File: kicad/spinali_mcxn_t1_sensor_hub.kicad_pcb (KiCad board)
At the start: 4 copper layers, 182 parts, among them J1 CAN1A, J10 Debug, J11 USB4105-GF-A, J2 CAN1B, J4 5055780421, J6 CAN0A, J7 CAN0B, J8 DF40TC-50DP-0.4V(51), J9 DF40TC-50DP-0.4V(51), Q1 BUK6D56-60EX, SW1 SW_SPST, U1 MPM3811GG-Z, U10 BMM350, U11 BMP581, U12 NX5P3363UKZ, U13 SK9822-EC20, U15 TJA1462ATK, U16 PCMF3USB3S, U17 LM74700, U2 MIC5504-1.8YMT, U3 LM5160DNTJ, U4 ICM-45686, U5 MCXN947VDFT, U6 NX5P3363UKZ, U7 TJA1103AHN, U8 TJA1462ATK, Y1 25MHz, Y2 32.768kHz, Y3 24MHz

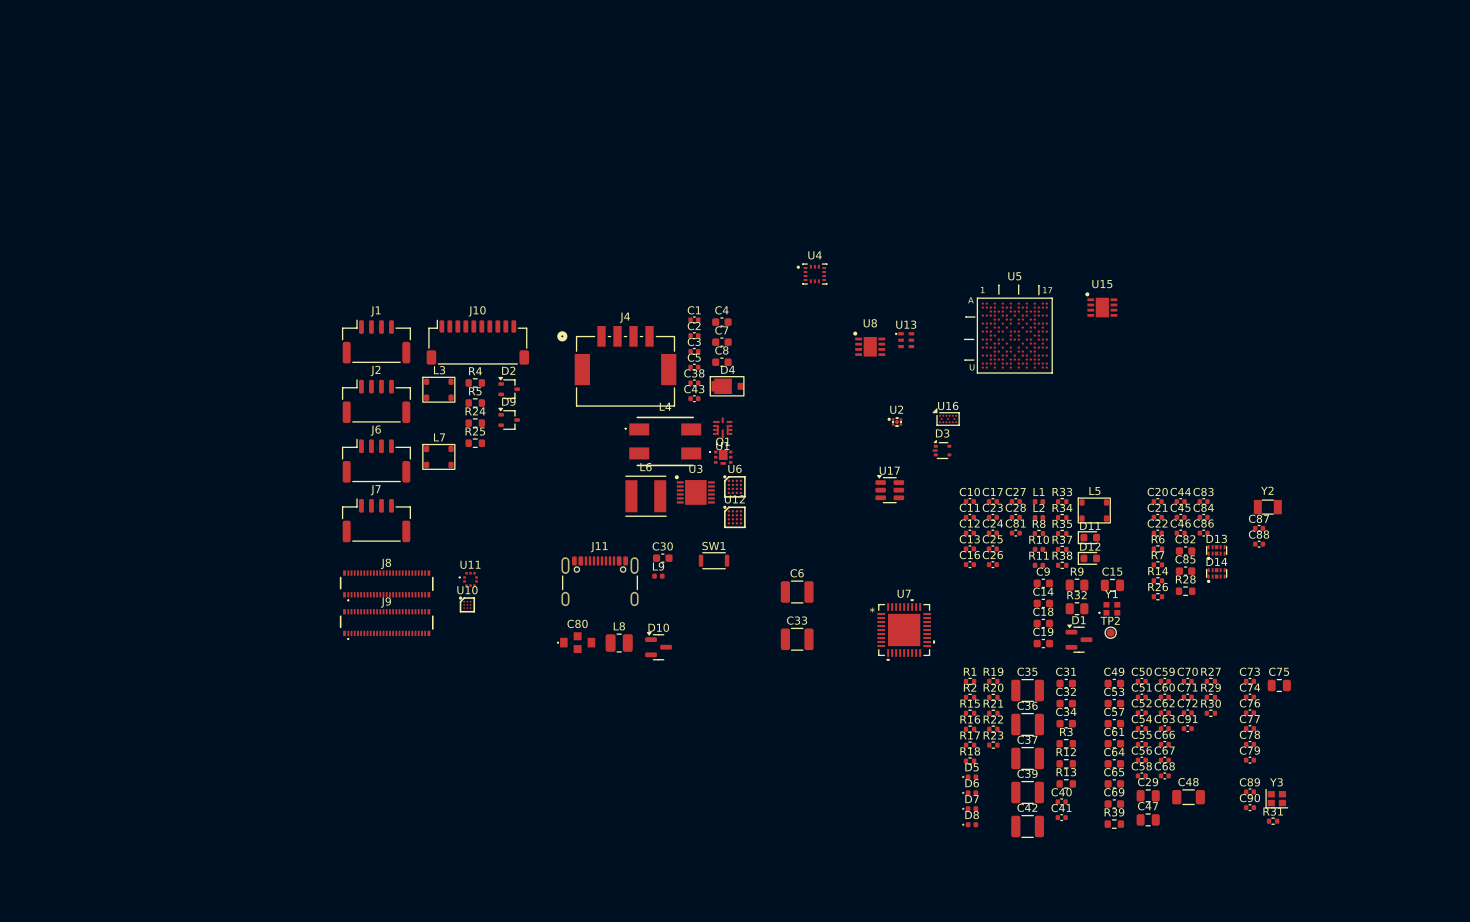
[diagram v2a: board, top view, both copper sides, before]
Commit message: Updated schematic and started on layout
- Implemented schematic changes after feedback:
	- BMM350 VDD is 1.8V
	- Replaced net labels with global labels for page references
	- Added 1uF cap to SK9822-EC20
- Added rev-RMII configuration for TJA1103 and DNP resistor to put it in slave mode
- Added TJA1103 PHY address info
- Changed decoupling caps for MCXN to smallest possible packages
- Added traces and vias at MCXN according to guidelines
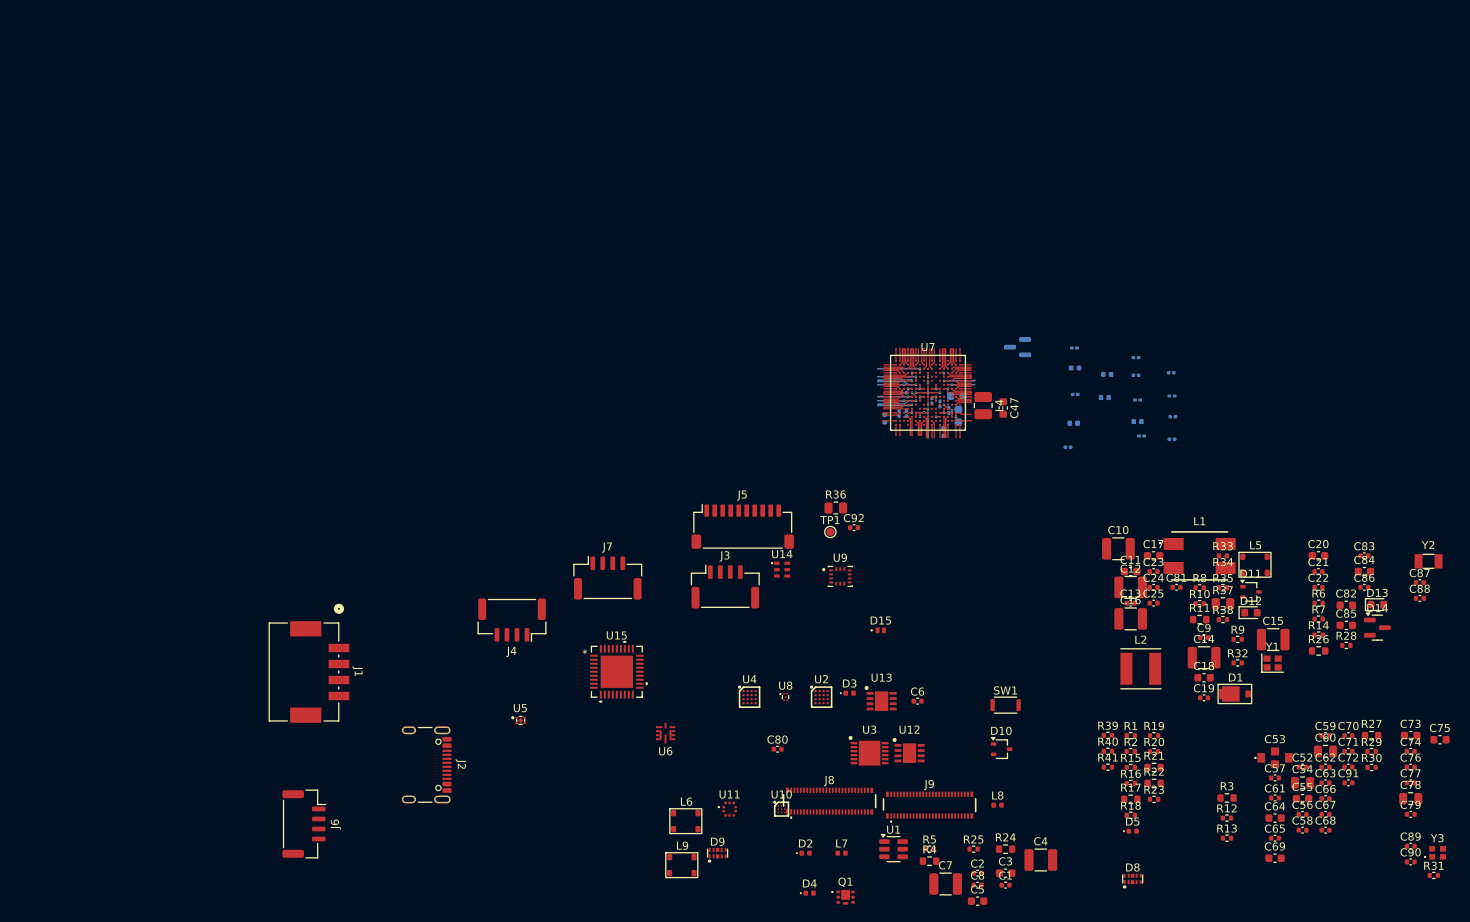
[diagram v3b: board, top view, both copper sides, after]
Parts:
- removed D7: 1V8-IND, LED_SMD:LED_0402_1005Metric
- removed J10: Debug, Connector_JST:JST_SH_SM10B-SRSS-TB_1x10-1MP_P1.00mm_Horizontal
- removed J11: USB4105-GF-A, Connector_USB:USB_C_Receptacle_GCT_USB4105-xx-A_16P_TopMnt_Horizontal
- removed TP2: ENET_REFCLK, TestPoint:TestPoint_Pad_D1.0mm
- removed U16: PCMF3USB3S, Package_CSP:Nexperia_WLCSP-15_6-3-6_2.37x1.17mm_Layout6x3_P0.4mm
- removed U17: LM74700, Package_TO_SOT_SMD:SOT-23-6
- added C92: 8pF 16V, Capacitor_SMD:C_0402_1005Metric, F.Cu at (139.8, 114.0)
- added D15: PESD5V0S1UL, TVS:PESD5V0S1ULD315, F.Cu at (143.1, 126.8)
- added J3: CAN0A, Connector_JST:JST_GH_SM04B-GHS-TB_1x04-1MP_P1.25mm_Horizontal, F.Cu at (123.7, 121.4)
- added J5: ~, Connector_JST:JST_SH_SM10B-SRSS-TB_1x10-1MP_P1.00mm_Horizontal, F.Cu at (125.8, 113.8)
- added R36: 1k 2/5W, Resistor_SMD:R_0805_2012Metric, F.Cu at (137.5, 111.5)
- added R40: 10k, Resistor_SMD:R_0402_1005Metric, F.Cu at (171.5, 141.9)
- added R41: 10k, Resistor_SMD:R_0402_1005Metric, F.Cu at (171.5, 143.9)
- added TP1: ENET_REFCLK, TestPoint:TestPoint_Pad_D1.0mm, F.Cu at (136.8, 114.5)
- added U14: SK9822-EC20, RGB_leds:SK9822EC20, F.Cu at (130.8, 119.2)
- added U9: ICM-45686, Sensors:IC_ICM-45686, F.Cu at (138.0, 120.0)
- C10: value 100nF 16V -> 10uF 100V; footprint Capacitor_SMD:C_0402_1005Metric -> Capacitor_SMD:C_1210_3225Metric
- C11: value 100nF 16V -> 100nF 100V; footprint Capacitor_SMD:C_0402_1005Metric -> Capacitor_SMD:C_0603_1608Metric
- C12, C16: value 100nF 16V -> 47uF 16V; footprint Capacitor_SMD:C_0402_1005Metric -> Capacitor_SMD:C_1210_3225Metric
- C14: value 1uF 16V -> 47uF 16V; footprint Capacitor_SMD:C_0603_1608Metric -> Capacitor_SMD:C_1210_3225Metric
- C15: value 10uF 16V -> 47uF 16V; footprint Capacitor_SMD:C_0805_2012Metric -> Capacitor_SMD:C_1210_3225Metric
- C17, C55, C73: value 100nF 16V -> 1uF 10V; footprint Capacitor_SMD:C_0402_1005Metric -> Capacitor_SMD:C_0603_1608Metric
- C18, C69: value 1uF 16V -> 1uF 10V
- C19: value 1uF 16V -> 22nF 10V; footprint Capacitor_SMD:C_0603_1608Metric -> Capacitor_SMD:C_0402_1005Metric
- C2: value 1nF 16V -> 1nF 100V
- C20: value 4700pF -> 1uF 25V; footprint Capacitor_SMD:C_0402_1005Metric -> Capacitor_SMD:C_0603_1608Metric
- C21: value 100pF -> 1nF 16V
- C22, C24: value 100pF -> 4.7pF 50V
- C23: value 100nF 50V -> 4.7pF 50V
- C25: value 4700pF 50V -> 4.7pF 50V
- C26: value 100pF -> 1uF 6.3V; moved to B.Cu
- C27: value 100nF 50V -> 100nF 10V; footprint Capacitor_SMD:C_0402_1005Metric -> Capacitor_SMD:C_0201_0603Metric; moved to B.Cu
- C28: value 8pF 16V -> 100nF 10V; footprint Capacitor_SMD:C_0402_1005Metric -> Capacitor_SMD:C_0201_0603Metric; moved to B.Cu
- C29: value 10uF 10V -> 100nF 10V; footprint Capacitor_SMD:C_0805_2012Metric -> Capacitor_SMD:C_0201_0603Metric; moved to B.Cu
- C3: value 10nF 16V -> 22nF 100V; footprint Capacitor_SMD:C_0402_1005Metric -> Capacitor_SMD:C_0603_1608Metric
- C30: value 1uF 10V -> 1uF 6.3V; footprint Capacitor_SMD:C_0603_1608Metric -> Capacitor_SMD:C_0402_1005Metric; moved to B.Cu
- C31, C34: value 100nF 100V -> 100nF 10V; footprint Capacitor_SMD:C_0603_1608Metric -> Capacitor_SMD:C_0201_0603Metric; moved to B.Cu
- C32: value 22nF 100V -> 100nF 10V; footprint Capacitor_SMD:C_0603_1608Metric -> Capacitor_SMD:C_0201_0603Metric; moved to B.Cu
- C33: value 10uF 100V -> 100nF 10V; footprint Capacitor_SMD:C_1210_3225Metric -> Capacitor_SMD:C_0201_0603Metric; moved to B.Cu
- C35, C37, C39, C42: value 47uF 16V -> 100nF 10V; footprint Capacitor_SMD:C_1210_3225Metric -> Capacitor_SMD:C_0201_0603Metric; moved to B.Cu
- C36: value 47uF 16V -> 1uF 6.3V; footprint Capacitor_SMD:C_1210_3225Metric -> Capacitor_SMD:C_0402_1005Metric; moved to B.Cu
- C38: value 1nF 100V -> 100nF 10V; footprint Capacitor_SMD:C_0402_1005Metric -> Capacitor_SMD:C_0201_0603Metric; moved to B.Cu
- C4: value 1uF 25V -> 10uF 100V; footprint Capacitor_SMD:C_0603_1608Metric -> Capacitor_SMD:C_1210_3225Metric
- C40, C41: value 100nF 16V -> 1uF 6.3V; moved to B.Cu
- C43: value 1nF 16V -> 100nF 10V; footprint Capacitor_SMD:C_0402_1005Metric -> Capacitor_SMD:C_0201_0603Metric; moved to B.Cu
- C44: value 100pF -> 100nF 10V; footprint Capacitor_SMD:C_0402_1005Metric -> Capacitor_SMD:C_0201_0603Metric; moved to B.Cu
- C45: value 4700pF -> 2.2uF 10V; moved to B.Cu
- C46: value 100pF -> 4.7uF 6.3V; footprint Capacitor_SMD:C_0402_1005Metric -> Capacitor_SMD:C_0603_1608Metric; moved to B.Cu
- C47: value 2.2uF 16V -> 10uF 6.3V; footprint Capacitor_SMD:C_0805_2012Metric -> Capacitor_SMD:C_0603_1608Metric
- C48: value 6.8uF 16V -> 100nF 10V; footprint Capacitor_SMD:C_1206_3216Metric -> Capacitor_SMD:C_0201_0603Metric; moved to B.Cu
- C49: value 1uF 16V -> 4.7uF 6.3V; moved to B.Cu
- C5: value 22nF 10V -> 100nF 100V; footprint Capacitor_SMD:C_0402_1005Metric -> Capacitor_SMD:C_0603_1608Metric
- C50, C51: value 100nF 16V -> 100nF 10V; footprint Capacitor_SMD:C_0402_1005Metric -> Capacitor_SMD:C_0201_0603Metric; moved to B.Cu
- C53: value 1uF 16V -> 15nF 50V; footprint Capacitor_SMD:C_0603_1608Metric -> Capacitors:NFM31HK103R1H3L
- C54: value 100nF 16V -> 10uF 10V; footprint Capacitor_SMD:C_0402_1005Metric -> Capacitor_SMD:C_0805_2012Metric
- C57, C61: value 1uF 16V -> 100nF 16V; footprint Capacitor_SMD:C_0603_1608Metric -> Capacitor_SMD:C_0402_1005Metric
- C6: value 10uF 100V -> 100nF 16V; footprint Capacitor_SMD:C_1210_3225Metric -> Capacitor_SMD:C_0402_1005Metric
- C60: value 100nF 16V -> 2.2uF 16V; footprint Capacitor_SMD:C_0402_1005Metric -> Capacitor_SMD:C_0805_2012Metric
- C63, C68: value 100nF 16V -> 47nF 10V
- C64: value 4.7uF 6.3V -> 1uF 10V
- C65: value 4.7uF 6.3V -> 100pF; footprint Capacitor_SMD:C_0603_1608Metric -> Capacitor_SMD:C_0402_1005Metric
- C66, C71: value 100nF 16V -> 4700pF
- C67, C70, C72: value 100nF 16V -> 100pF
- C7: value 1uF 10V -> 47uF 16V; footprint Capacitor_SMD:C_0603_1608Metric -> Capacitor_SMD:C_1210_3225Metric
- C75: value 2.2uF 16V -> 1uF 16V; footprint Capacitor_SMD:C_0805_2012Metric -> Capacitor_SMD:C_0603_1608Metric
- C78: value 100nF 16V -> 10uF 16V; footprint Capacitor_SMD:C_0402_1005Metric -> Capacitor_SMD:C_0805_2012Metric
- C8: value 1uF 10V -> 1nF 16V; footprint Capacitor_SMD:C_0603_1608Metric -> Capacitor_SMD:C_0402_1005Metric
- C80: value 15nF 50V -> 100nF 16V; footprint Capacitors:NFM31HK103R1H3L -> Capacitor_SMD:C_0402_1005Metric
- C81: value 8pF 16V -> 100nF 16V
- C82, C85: value 1uF 10V -> 1uF 16V
- C83: value 47nF 10V -> 100nF 16V
- C84: value 47nF 10V -> 1uF 16V; footprint Capacitor_SMD:C_0402_1005Metric -> Capacitor_SMD:C_0603_1608Metric
- C86: value 100nF 16V -> 100nF 50V
- C87, C89: value 4.7pF 50V -> 100pF
- C88: value 4.7pF 50V -> 4700pF 50V
- C9: value 1uF 16V -> 10nF 16V; footprint Capacitor_SMD:C_0603_1608Metric -> Capacitor_SMD:C_0402_1005Metric
- C90: value 4.7pF 50V -> 100nF 50V
- C91: value 100nF 16V -> 8pF 16V
- D1: value VETH100A203S-G3-18 -> 6DFN62CA-M3/I; footprint Package_TO_SOT_SMD:SOT-23 -> Diodes:DFN3820A
- D10: value BAT54C -> PESD2IVN24-UX; footprint Package_TO_SOT_SMD:SOT-23 -> Package_TO_SOT_SMD:SOT-323_SC-70
- D11: value LED_AMB -> PESD2IVN24-UX; footprint LED_SMD:LED_0603_1608Metric -> Package_TO_SOT_SMD:SOT-323_SC-70
- D12: value LED_GRN -> LED_AMB
- D13: value ESD7104MUTAG -> LED_GRN; footprint TVS:ESD8104MUTAG -> LED_SMD:LED_0603_1608Metric
- D14: value ESD7104MUTAG -> VETH100A203S-G3-18; footprint TVS:ESD8104MUTAG -> Package_TO_SOT_SMD:SOT-23
- D2: value PESD2IVN24-UX -> VBUS; footprint Package_TO_SOT_SMD:SOT-323_SC-70 -> LED_SMD:LED_0402_1005Metric
- D3: value PESD5V0L4UW -> 3V3-IND; footprint Package_TO_SOT_SMD:SOT-665 -> LED_SMD:LED_0402_1005Metric
- D4: value 6DFN62CA-M3/I -> 1V8-IND; footprint Diodes:DFN3820A -> LED_SMD:LED_0402_1005Metric
- D6: value 3V3-IND -> BAT54C; footprint LED_SMD:LED_0402_1005Metric -> Package_TO_SOT_SMD:SOT-23; moved to B.Cu
- D8: value VBUS -> ESD7104MUTAG; footprint LED_SMD:LED_0402_1005Metric -> TVS:ESD8104MUTAG
- D9: value PESD2IVN24-UX -> ESD7104MUTAG; footprint Package_TO_SOT_SMD:SOT-323_SC-70 -> TVS:ESD8104MUTAG
- J1: value CAN1A -> 5055780421; footprint Connector_JST:JST_GH_SM04B-GHS-TB_1x04-1MP_P1.25mm_Horizontal -> Connectors:CONN_5055780421_MOL
- J2: value CAN1B -> USB4105-GF-A; footprint Connector_JST:JST_GH_SM04B-GHS-TB_1x04-1MP_P1.25mm_Horizontal -> Connector_USB:USB_C_Receptacle_GCT_USB4105-xx-A_16P_TopMnt_Horizontal
- J4: value 5055780421 -> CAN0B; footprint Connectors:CONN_5055780421_MOL -> Connector_JST:JST_GH_SM04B-GHS-TB_1x04-1MP_P1.25mm_Horizontal
- J6: value CAN0A -> CAN1A
- J7: value CAN0B -> CAN1B
- L1: value 600 Ohm -> ACM7060-301-2PL-TL01; footprint Inductor_SMD:L_0402_1005Metric -> Inductors:ACM70603012PLTL01
- L2: value 600 Ohm -> 33uH 1.3A; footprint Inductor_SMD:L_0402_1005Metric -> Inductors:VLS5045EX330M
- L3: value IFLN1210BEER512N -> 120 Ohm; footprint Inductors:IFLN1210BEER512N -> Inductor_SMD:L_0402_1005Metric; moved to B.Cu
- L4: value ACM7060-301-2PL-TL01 -> 1.5uH; footprint Inductors:ACM70603012PLTL01 -> Inductor_SMD:L_1008_2520Metric
- L6: value VLS5045EX-330M-H -> IFLN1210BEER512N; footprint Inductors:VLS5045EX330M -> Inductors:IFLN1210BEER512N
- L7: value IFLN1210BEER512N -> 600 Ohm; footprint Inductors:IFLN1210BEER512N -> Inductor_SMD:L_0402_1005Metric
- L8: value 1.5uH -> 600 Ohm; footprint Inductor_SMD:L_1008_2520Metric -> Inductor_SMD:L_0402_1005Metric
- L9: value 120 Ohm -> IFLN1210BEER512N; footprint Inductor_SMD:L_0402_1005Metric -> Inductors:IFLN1210BEER512N
- R1: value 3k3 -> 2k2
- R10: value 680 -> 2k2; footprint Inductor_SMD:L_0402_1005Metric -> Resistor_SMD:R_0402_1005Metric
- R11: value 680 -> 12k 75V; footprint Inductor_SMD:L_0402_1005Metric -> Resistor_SMD:R_0603_1608Metric
- R12: value 68k 75V -> 2k2; footprint Resistor_SMD:R_0603_1608Metric -> Resistor_SMD:R_0402_1005Metric
- R13: value 12k 75V -> 18k 1%; footprint Resistor_SMD:R_0603_1608Metric -> Resistor_SMD:R_0402_1005Metric
- R14: value 0 -> 39k 1%
- R15, R16: value 1k -> 10k
- R17: value 82k 1% -> 100; footprint Resistor_SMD:R_0402_1005Metric -> Resistor_SMD:R_0603_1608Metric
- R18: value 18k 1% -> 5.1k
- R19: value 100k -> 5.1k
- R2: value 2k2 -> 24k 1%
- R20: value 2k2 -> 0
- R21: value 47k 1% -> 60.4R 1% 1/3W; footprint Resistor_SMD:R_0402_1005Metric -> Resistor_SMD:R_0603_1608Metric
- R22: value 2k2 -> 60.4R 1% 1/3W; footprint Resistor_SMD:R_0402_1005Metric -> Resistor_SMD:R_0603_1608Metric
- R23: value 24k 1% -> 0
- R24: value 60.4R 1% 1/3W -> 100
- R25: value 60.4R 1% 1/3W -> 0; footprint Resistor_SMD:R_0603_1608Metric -> Resistor_SMD:R_0402_1005Metric
- R26: value 0 -> 60.4R 1% 1/3W; footprint Resistor_SMD:R_0402_1005Metric -> Resistor_SMD:R_0603_1608Metric
- R27: value 10k -> 60.4R 1% 1/3W; footprint Resistor_SMD:R_0402_1005Metric -> Resistor_SMD:R_0603_1608Metric
- R28: value 100 -> 0; footprint Resistor_SMD:R_0603_1608Metric -> Resistor_SMD:R_0402_1005Metric
- R29, R30: value 5.1k -> 10k
- R32: value 1k 2/5W -> 10k; footprint Resistor_SMD:R_0805_2012Metric -> Resistor_SMD:R_0402_1005Metric
- R33: value 0 -> 680; footprint Resistor_SMD:R_0402_1005Metric -> Inductor_SMD:L_0402_1005Metric
- R34: value 10k -> 680; footprint Resistor_SMD:R_0402_1005Metric -> Inductor_SMD:L_0402_1005Metric
- R35, R38: value 10k -> 0
- R37: value 10k -> 1k 2/5W; footprint Resistor_SMD:R_0402_1005Metric -> Resistor_SMD:R_0805_2012Metric
- R39: value 100 -> 10k; footprint Resistor_SMD:R_0603_1608Metric -> Resistor_SMD:R_0402_1005Metric
- R4: value 60.4R 1% 1/3W -> 68k 75V
- R5: value 60.4R 1% 1/3W -> 3k3; footprint Resistor_SMD:R_0603_1608Metric -> Resistor_SMD:R_0402_1005Metric
- R6: value 0 -> 100k
- R7: value 0 -> 82k 1%
- R8: value 0 -> 1k
- R9: value 1k 2/5W -> 1k; footprint Resistor_SMD:R_0805_2012Metric -> Resistor_SMD:R_0402_1005Metric
- U1: value MPM3811GG-Z -> LM74700; footprint Power:QFN2x2x1p6_MPM3811_MNP -> Package_TO_SOT_SMD:SOT-23-6
- U12: value NX5P3363UKZ -> TJA1462ATK; footprint NXP_BGA:BGA16C50P4X4_220X220X60 -> NXP_HV:SON65P300X300X100-9N-D
- U13: value SK9822-EC20 -> TJA1462ATK; footprint RGB_leds:SK9822EC20 -> NXP_HV:SON65P300X300X100-9N-D
- U15: value TJA1462ATK -> TJA1103AHN; footprint NXP_HV:SON65P300X300X100-9N-D -> NXP_HV:HVQFN36_SOT1092-2_NXP
- U2: value MIC5504-1.8YMT -> NX5P3363UKZ; footprint Power:VREG_MIC5504-3.3YMT-TZ -> NXP_BGA:BGA16C50P4X4_220X220X60
- U4: value ICM-45686 -> NX5P3363UKZ; footprint Sensors:IC_ICM-45686 -> NXP_BGA:BGA16C50P4X4_220X220X60
- U5: value MCXN947VDFT -> MIC5504-1.8YMT; footprint NXP_BGA:BGA184_0P5_9X9_SM -> Power:VREG_MIC5504-3.3YMT-TZ
- U6: value NX5P3363UKZ -> MPM3811GG-Z; footprint NXP_BGA:BGA16C50P4X4_220X220X60 -> Power:QFN2x2x1p6_MPM3811_MNP
- U7: value TJA1103AHN -> MCXN947VDFT; footprint NXP_HV:HVQFN36_SOT1092-2_NXP -> NXP_BGA:BGA184_0P5_9X9_SM
- U8: value TJA1462ATK -> PCMF1USB3SZ; footprint NXP_HV:SON65P300X300X100-9N-D -> TVS:PESD1USB3BCX
- Y1: value 25MHz -> 24MHz; footprint Crystals:XRCGB25M000F3A00R0 -> Crystal:Crystal_SMD_2016-4Pin_2.0x1.6mm
- Y3: value 24MHz -> 25MHz; footprint Crystal:Crystal_SMD_2016-4Pin_2.0x1.6mm -> Crystals:XRCGB25M000F3A00R0
- moved R24 85.0 mm to (158.7, 154.1)
- moved R4 82.5 mm to (149.2, 155.6)
- moved L3 81.0 mm to (167.2, 100.9), turned to 180 degrees
- moved C1 80.7 mm to (158.7, 158.6)
- moved R25 80.3 mm to (154.7, 154.1)
- moved R5 79.6 mm to (149.2, 154.1)
- moved U5 78.3 mm to (98.1, 138.1)
- moved C4 78.2 mm to (163.1, 155.5)
- moved C2 75.9 mm to (155.2, 157.1)
- moved C3 75.9 mm to (158.7, 157.1)
- moved U15 75.9 mm to (110.1, 132.0)
- moved C5 75.6 mm to (155.2, 160.6)
- moved C7 73.3 mm to (151.2, 158.5)
- moved C8 72.8 mm to (155.2, 158.6)
- moved L7 72.4 mm to (138.2, 154.6)
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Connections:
- net /Board-to-Board/P0_23/FLEXIO0_D7 renamed P0_23/FLEXIO0_D7
- C1 pad 1: Net-(Q1-S) -> Net-(C1-Pad1)
- C10 pad 2: VDDIO -> +BATT
- C11 pad 2: VDDIO -> +BATT
- C12 pad 1: Net-(U7-VDDA_AO) -> GND
- C12 pad 2: GND -> Net-(U4-EN)
- C13 pad 1: GND -> Net-(U4-EN)
- C13 pad 2: Net-(U7-VDDA_AO) -> GND
- C14 pad 2: Net-(U7-VDDA_AO) -> +5V
- C15 pad 2: Net-(U7-VDD_CORE) -> +5V
- C16 pad 2: Net-(U7-VDD_CORE) -> +3V3
- C17 pad 1: GND -> +3V3
- C17 pad 2: VDDA_TRX -> GND
- C18 pad 1: GND -> +1V8
- C18 pad 2: VDDA_TRX -> GND
- C19 pad 2: VDDA_TRX -> Net-(U3-SS)
- C2 pad 1: GND -> Net-(Q1-S)
- C2 pad 2: Net-(U6-CAP) -> GND
- C20 pad 2: Net-(C20-Pad2) -> Net-(U3-VCC)
- C21 pad 1: Net-(D9-A2) -> GND
- C21 pad 2: GND -> Net-(U4-CAP)
- C22 pad 2: Net-(D9-A1) -> /MCU IO Part 1/XTAL48M
- C23 pad 1: Net-(C23-Pad1) -> GND
- C23 pad 2: /Ethernet PHY/ENET_TRX_P -> /MCU IO Part 1/EXTAL48M
- C24 pad 1: GND -> /MCU IO Part 2/P5_0/EXTAL32K
- C24 pad 2: /Ethernet PHY/ENET_TRX_P -> GND
- C25 pad 1: GND -> /MCU IO Part 2/P5_1/XTAL32K
- C25 pad 2: Net-(C25-Pad2) -> GND
- C26 pad 1: /Ethernet PHY/ENET_TRX_M -> +3V3
- C27 pad 1: Net-(C27-Pad1) -> +3V3
- C27 pad 2: /Ethernet PHY/ENET_TRX_M -> GND
- C28 pad 1: /Ethernet PHY/ENET0_XTAL_IN -> +3V3
- C29 pad 1: VBUS -> +3V3
- C3 pad 1: Net-(U3-BST) -> GND
- C3 pad 2: Net-(C3-Pad2) -> Net-(Q1-S)
- C30 pad 1: VBUS -> +3V3
- C31 pad 1: Net-(U17-VCAP) -> +3V3
- C31 pad 2: Net-(Q1-S) -> GND
- C32 pad 1: GND -> +3V3
- C32 pad 2: Net-(Q1-S) -> GND
- C33 pad 2: +BATT -> +3V3
- C34 pad 2: +BATT -> Net-(U7H-VDD_BAT)
- C35 pad 2: Net-(U6-EN) -> Net-(U7H-VDD_ANA)
- C36 pad 1: GND -> +3V3
- C36 pad 2: +3V3 -> GND
- C37 pad 1: GND -> +3V3
- C37 pad 2: +5V -> GND
- C38 pad 1: Net-(C38-Pad1) -> +3V3
- C39 pad 1: GND -> +3V3
- C39 pad 2: +5V -> GND
- C4 pad 2: Net-(U3-VCC) -> +BATT
- C40 pad 1: Net-(U6-EN) -> GND
- C40 pad 2: GND -> Net-(U7H-VDD_ANA)
- C41 pad 1: VBUS -> +3V3
- C42 pad 1: GND -> +3V3
- C42 pad 2: +5V -> GND
- C43 pad 1: GND -> +3V3
- C43 pad 2: Net-(U12-CAP) -> GND
- C44 pad 2: Net-(D2-A1) -> +3V3
- C45 pad 1: GND -> Net-(U7H-VDD_SYS/VOUT_SYS)
- C45 pad 2: Net-(C45-Pad2) -> GND
- C46 pad 1: Net-(D2-A2) -> +3V3
- C47 pad 1: Net-(U5H-VDD_SYS/VOUT_SYS) -> Net-(U7H-VDD_CORE_1)
- C48 pad 1: Net-(U5H-VDD_CORE_1) -> GND
- C48 pad 2: GND -> Net-(U7H-VDD_CORE_1)
- C49 pad 1: +3V3 -> Net-(U7H-VDD_CORE_1)
- C5 pad 1: GND -> Net-(U1-VCAP)
- C5 pad 2: Net-(U3-SS) -> Net-(Q1-S)
- C50 pad 1: +3V3 -> Net-(U7H-VDD_CORE_1)
- C51 pad 1: +3V3 -> Net-(U7H-VDD_CORE_1)
- C52 pad 1: +3V3 -> RESET_b
- C53 pad 1: +3V3 -> Net-(D15-K1)
- C54 pad 1: +3V3 -> VBUS
- C55 pad 1: +3V3 -> VBUS
- C56 pad 1: GND -> +3V3
- C56 pad 2: +3V3 -> GND
- C59 pad 1: +3V3 -> +1V8
- C6 pad 1: GND -> VBUS
- C6 pad 2: +BATT -> GND
- C60 pad 1: +3V3 -> Net-(U10-CRST)
- C61 pad 1: +3V3 -> GND
- C61 pad 2: GND -> +3V3
- C62 pad 1: +3V3 -> GND
- C62 pad 2: GND -> +3V3
- C64 pad 1: +3V3 -> +5V
- C65 pad 1: Net-(U5H-VDD_CORE_1) -> GND
- C65 pad 2: GND -> Net-(D10-A1)
- C66 pad 1: Net-(U5H-VDD_CORE_1) -> GND
- C66 pad 2: GND -> Net-(C66-Pad2)
- C67 pad 1: Net-(U5H-VDD_CORE_1) -> Net-(D10-A2)
- C68 pad 1: GND -> +3V3
- C68 pad 2: Net-(U5H-VDD_CORE_1) -> GND
- C69 pad 1: GND -> +5V
- C69 pad 2: Net-(U5H-VDD_ANA) -> GND
- C7 pad 1: +3V3 -> GND
- C7 pad 2: GND -> +5V
- C70 pad 2: Net-(U5H-VDD_ANA) -> Net-(D11-A1)
- C71 pad 2: +3V3 -> Net-(C71-Pad2)
- C72 pad 1: GND -> Net-(D11-A2)
- C72 pad 2: Net-(U5H-VDD_BAT) -> GND
- C73 pad 2: +3V3 -> +5V
- C74 pad 2: +3V3 -> +5V
- C75 pad 1: Net-(U10-CRST) -> GND
- C75 pad 2: GND -> VDDIO
- C76 pad 1: +3V3 -> GND
- C76 pad 2: GND -> VDDIO
- C77 pad 1: +3V3 -> GND
- C77 pad 2: GND -> VDDIO
- C78 pad 1: +3V3 -> GND
- C78 pad 2: GND -> Net-(U15-VDD_CORE)
- C79 pad 1: +3V3 -> GND
- C79 pad 2: GND -> Net-(U15-VDD_CORE)
- C8 pad 1: +1V8 -> GND
- C8 pad 2: GND -> Net-(U2-CAP)
- C80 pad 1: Net-(D3A-K1) -> Net-(U15-VDDA_AO)
- C81 pad 1: /Ethernet PHY/ENET0_XTAL_OUT -> GND
- C81 pad 2: GND -> Net-(U15-VDDA_AO)
- C82 pad 1: +5V -> GND
- C82 pad 2: GND -> Net-(U15-VDDA_AO)
- C83 pad 1: +3V3 -> GND
- C83 pad 2: GND -> VDDA_TRX
- C84 pad 1: +3V3 -> GND
- C84 pad 2: GND -> VDDA_TRX
- C85 pad 1: +5V -> GND
- C85 pad 2: GND -> VDDA_TRX
- C86 pad 1: +5V -> Net-(C86-Pad1)
- C86 pad 2: GND -> ENET0_TRX_P
- C87 pad 1: /MCU IO Part 2/P5_1/XTAL32K -> GND
- C87 pad 2: GND -> ENET0_TRX_P
- C88 pad 1: /MCU IO Part 2/P5_0/EXTAL32K -> GND
- C88 pad 2: GND -> Net-(C88-Pad2)
- C89 pad 1: GND -> ENET0_TRX_M
- C89 pad 2: /MCU IO Part 1/XTAL48M -> GND
- C9 pad 1: GND -> Net-(U3-BST)
- C9 pad 2: VDDIO -> Net-(C9-Pad2)
- C90 pad 1: GND -> Net-(C90-Pad1)
- C90 pad 2: /MCU IO Part 1/EXTAL48M -> ENET0_TRX_M
- C91 pad 1: /MCU IO USB & Power/RESET_b -> /Ethernet PHY/ENET0_XTAL_IN
- D1 pad 1: /Ethernet PHY/ENET_TRX_P -> GND
- D1 pad 2: /Ethernet PHY/ENET_TRX_M -> Net-(C1-Pad1)
- D10 pad 1: /MCU IO USB & Power/VDD_BAT -> Net-(D10-A1)
- D10 pad 2: +3V3 -> Net-(D10-A2)
- D10 pad 3: Net-(U5H-VDD_BAT) -> GND
- D11 pad 1: GND -> Net-(D11-A1)
- D11 pad 2: Net-(D11-A) -> Net-(D11-A2)
- D13 pad 1: /Communication/P0_1/DEBUG_TCLK_SWCLK -> GND
- D13 pad 2: /Communication/P0_0/DEBUG_TMS_SWDIO -> Net-(D13-A)
- D14 pad 1: /Communication/RESET_b -> ENET0_TRX_P
- D14 pad 2: /Communication/P0_4 -> ENET0_TRX_M
- D2 pad 1: Net-(D2-A1) -> GND
- D2 pad 2: Net-(D2-A2) -> Net-(D2-A)
- D3 pad 1: Net-(D3A-K1) -> GND
- D3 pad 2: GND -> Net-(D3-A)
- D4 pad 2: Net-(C38-Pad1) -> Net-(D4-A)
- D6 pad 1: GND -> VDD_BAT
- D6 pad 2: Net-(D6-A) -> +3V3
- D8 pad 1: GND -> P0_1/DEBUG_TCLK_SWCLK
- D8 pad 2: Net-(D8-A) -> P0_0/DEBUG_TMS_SWDIO
- D9 pad 1: Net-(D9-A1) -> RESET_b
- D9 pad 2: Net-(D9-A2) -> P0_4
- J1 pad 1: Net-(J1-Pin_1) -> Net-(C1-Pad1)
- J1 pad 2: Net-(D9-A1) -> ENET0_TRX_P
- J1 pad 3: Net-(D9-A2) -> ENET0_TRX_M
- J4 pad 1: Net-(C38-Pad1) -> Net-(J3-Pad1)
- J4 pad 2: /Power supplies/ENET_TRX_P -> Net-(D10-A1)
- J4 pad 3: /Power supplies/ENET_TRX_M -> Net-(D10-A2)
- J6 pad 2: Net-(D2-A1) -> Net-(D11-A1)
- J6 pad 3: Net-(D2-A2) -> Net-(D11-A2)
- J6 pad MP: (no net) -> GND
- J7 pad 2: Net-(D2-A1) -> Net-(D11-A1)
- J7 pad 3: Net-(D2-A2) -> Net-(D11-A2)
- J7 pad MP: (no net) -> GND
- J8 pad 11: /Board-to-Board/VDD_BAT -> VDD_BAT
- J8 pad 14: /Board-to-Board/P1_8/I3C1_SDA/FC4_P0 -> P1_8/I3C1_SDA/FC4_P0
- J8 pad 16: /Board-to-Board/P1_9/I3C1_SCL/FC4_P1 -> P1_9/I3C1_SCL/FC4_P1
- J8 pad 20: /Board-to-Board/P1_22/FC4_P2 -> P1_22/FC4_P2
- J8 pad 21: /Board-to-Board/P4_0/FC2_P0 -> P4_0/FC2_P0
- J8 pad 22: /Board-to-Board/P1_23/FC4_P3 -> P1_23/FC4_P3
- J8 pad 23: /Board-to-Board/P4_1/FC2_P1 -> P4_1/FC2_P1
- J8 pad 26: /Board-to-Board/P3_1/FC6_P0 -> P3_1/FC6_P0
- J8 pad 27: /Board-to-Board/P4_2/FC2_P2 -> P4_2/FC2_P2
- J8 pad 28: /Board-to-Board/P3_6/FC6_P1 -> P3_6/FC6_P1
- J8 pad 29: /Board-to-Board/P4_3/FC2_P3 -> P4_3/FC2_P3
- J8 pad 32: /Board-to-Board/P3_10/FC6_P2 -> P3_10/FC6_P2
- J8 pad 33: /Board-to-Board/P4_23/FC2_P6 -> P4_23/FC2_P6
- J8 pad 34: /Board-to-Board/P3_11/FC6_P3 -> P3_11/FC6_P3
- J8 pad 35: /Board-to-Board/P4_20/FC2_P4 -> P4_20/FC2_P4
- J8 pad 38: /Board-to-Board/P3_18/FC6_P6 -> P3_18/FC6_P6
- J8 pad 39: /Board-to-Board/ANA_22/OPAMP2_INN -> ANA_22/OPAMP2_INN
- J8 pad 40: /Board-to-Board/P3_13/FC6_P5 -> P3_13/FC6_P5
- J8 pad 41: /Board-to-Board/ANA_6/DAC2_OUT -> ANA_6/DAC2_OUT
- J8 pad 44: /Board-to-Board/P2_10/TRACE_DATA2 -> P2_10/TRACE_DATA2
- J8 pad 46: /Board-to-Board/P2_11/TRACE_DATA3 -> P2_11/TRACE_DATA3
- J8 pad 47: /Board-to-Board/P3_21/FLEXIO0_D29 -> P3_21/FLEXIO0_D29
- J9 pad 10: /Board-to-Board/P3_8/SmartDMA_PIO8 -> P3_8/SmartDMA_PIO8
- J9 pad 11: /Board-to-Board/P2_2/SDHC0_D1 -> P2_2/SDHC0_D1
- J9 pad 12: /Board-to-Board/P3_9/SmartDMA_PIO9 -> P3_9/SmartDMA_PIO9
- J9 pad 15: /Board-to-Board/P2_7/SDHC0_D2 -> P2_7/SDHC0_D2
- J9 pad 16: /Board-to-Board/P1_0/FC3_P0 -> P1_0/FC3_P0
- J9 pad 17: /Board-to-Board/P2_6/SDHC0_D3 -> P2_6/SDHC0_D3
- J9 pad 18: /Board-to-Board/P1_1/FC3_P1 -> P1_1/FC3_P1
- J9 pad 21: /Board-to-Board/P2_1/SDHC0_D4 -> P2_1/SDHC0_D4
- J9 pad 22: /Board-to-Board/P1_2/FC3_P2 -> P1_2/FC3_P2
- J9 pad 23: /Board-to-Board/P2_0/SDHC0_D5 -> P2_0/SDHC0_D5
- J9 pad 24: /Board-to-Board/P1_3/FC3_P3 -> P1_3/FC3_P3
- J9 pad 27: /Board-to-Board/P2_9/SDHC0_D6 -> P2_9/SDHC0_D6
- J9 pad 28: /Board-to-Board/P1_18/FC3_P6 -> P1_18/FC3_P6
- J9 pad 29: /Board-to-Board/P2_8/SDHC0_D7 -> P2_8/SDHC0_D7
- J9 pad 3: /Board-to-Board/P2_5/SDHC0_CMD -> P2_5/SDHC0_CMD
- J9 pad 32: /Board-to-Board/P1_16/FC3_P4 -> P1_16/FC3_P4
- J9 pad 33: /Board-to-Board/P3_2/FC7_P0 -> P3_2/FC7_P0
- J9 pad 34: /Board-to-Board/P1_17/FC3_P5 -> P1_17/FC3_P5
- J9 pad 35: /Board-to-Board/P3_3/FC7_P1 -> P3_3/FC7_P1
- J9 pad 38: /Board-to-Board/P0_16/FC0_P0 -> P0_16/FC0_P0
- J9 pad 39: /Board-to-Board/P3_4/FC7_P2 -> P3_4/FC7_P2
- J9 pad 4: /Board-to-Board/P3_0/SmartDMA_PIO0 -> P3_0/SmartDMA_PIO0
- J9 pad 40: /Board-to-Board/P0_17/FC0_P1 -> P0_17/FC0_P1
- J9 pad 41: /Board-to-Board/P3_5/FC7_P3 -> P3_5/FC7_P3
- J9 pad 44: /Board-to-Board/P0_18/FC0_P2 -> P0_18/FC0_P2
- J9 pad 45: /Board-to-Board/P3_19/FC7_P6 -> P3_19/FC7_P6
- J9 pad 46: /Board-to-Board/P0_7/FC0_P3 -> P0_7/FC0_P3
- J9 pad 47: /Board-to-Board/P3_12/FC7_P4 -> P3_12/FC7_P4
- J9 pad 48: /Board-to-Board/P0_22/FC0_P6 -> P0_22/FC0_P6
- J9 pad 5: /Board-to-Board/P2_4/SDHC0_CLK -> P2_4/SDHC0_CLK
- J9 pad 6: /Board-to-Board/P3_7/SmartDMA_PIO7 -> P3_7/SmartDMA_PIO7
- J9 pad 9: /Board-to-Board/P2_3/SDHC0_D0 -> P2_3/SDHC0_D0
- L1 pad 1: +3V3 -> Net-(C1-Pad1)
- L1 pad 2: VDDIO -> GND
- L2 pad 1: +3V3 -> Net-(C9-Pad2)
- L2 pad 2: Net-(U7-VDDA_AO) -> Net-(U4-EN)
- L3 pad 1: Net-(U8-CANH) -> +3V3
- L3 pad 2: Net-(D2-A1) -> Net-(U7H-VDD_ANA)
- L4 pad 1: Net-(C38-Pad1) -> Net-(U7H-VDD_CORE_1)
- L4 pad 2: GND -> Net-(U7H-DCDC_LX/DCDC_LX)
- L5 pad 1: /Ethernet PHY/TRX_P -> Net-(U12-CANH)
- L5 pad 2: Net-(C23-Pad1) -> Net-(D10-A1)
- L5 pad 3: Net-(C27-Pad1) -> Net-(D10-A2)
- L5 pad 4: /Ethernet PHY/TRX_M -> Net-(U12-CANL)
- L6 pad 1: Net-(C3-Pad2) -> Net-(U13-CANH)
- L6 pad 2: Net-(U6-EN) -> Net-(D11-A1)
- L7 pad 1: Net-(U15-CANH) -> +3V3
- L7 pad 2: Net-(D9-A1) -> VDDIO
- L8 pad 1: Net-(U5H-VDD_CORE_1) -> +3V3
- L8 pad 2: Net-(U5H-DCDC_LX/DCDC_LX) -> Net-(U15-VDDA_AO)
- L9 pad 1: +3V3 -> /Ethernet PHY/TRX_P
- L9 pad 2: Net-(U5H-VDD_ANA) -> Net-(C86-Pad1)
- R1 pad 1: Net-(U6-EN) -> VBUS
- R1 pad 2: Net-(U3-FB) -> Net-(D2-A)
- R10 pad 1: Net-(U7-TMS/GPIO0/CONFIG0) -> Net-(U4-EN)
- R10 pad 2: Net-(D11-A) -> Net-(D5-A)
- R11 pad 1: Net-(U7-TDI/GPIO1) -> Net-(U3-EN/UVLO)
- R11 pad 2: Net-(D12-A) -> GND
- R12 pad 1: +BATT -> Net-(U3-FB)
- R12 pad 2: Net-(U3-EN/UVLO) -> GND
- R13 pad 1: Net-(U3-EN/UVLO) -> Net-(U6-FB)
- R14 pad 1: Net-(U8-CANH) -> Net-(U4-ILIM)
- R14 pad 2: Net-(D2-A1) -> GND
- R15 pad 1: +1V8 -> +3V3
- R15 pad 2: Net-(D7-A) -> /MCU IO Part 1/P0_6/ISPMODE_N
- R16 pad 2: Net-(D6-A) -> RESET_b
- R17 pad 1: +3V3 -> Net-(U7G-RESET_b)
- R17 pad 2: Net-(U1-FB) -> RESET_b
- R18 pad 1: Net-(U1-FB) -> Net-(J2-CC1)
- R19 pad 1: +5V -> GND
- R19 pad 2: Net-(U1-EN) -> Net-(J2-CC2)
- R2 pad 1: Net-(U3-FB) -> Net-(U2-ILIM)
- R20 pad 1: Net-(U6-EN) -> Net-(U12-CANH)
- R20 pad 2: Net-(D5-A) -> Net-(D10-A1)
- R21 pad 1: Net-(U6-ILIM) -> Net-(D10-A1)
- R21 pad 2: GND -> Net-(C66-Pad2)
- R22 pad 1: VBUS -> Net-(C66-Pad2)
- R22 pad 2: Net-(D8-A) -> Net-(D10-A2)
- R23 pad 1: Net-(U12-ILIM) -> Net-(D10-A2)
- R23 pad 2: GND -> Net-(U12-CANL)
- R24 pad 1: Net-(D2-A1) -> +3V3
- R24 pad 2: Net-(C45-Pad2) -> Net-(J5-Pad1)
- R25 pad 1: Net-(C45-Pad2) -> Net-(U13-CANH)
- R25 pad 2: Net-(D2-A2) -> Net-(D11-A1)
- R26 pad 1: Net-(D2-A2) -> Net-(D11-A1)
- R26 pad 2: Net-(U8-CANL) -> Net-(C71-Pad2)
- R27 pad 1: +3V3 -> Net-(C71-Pad2)
- R27 pad 2: /MCU IO USB & Power/RESET_b -> Net-(D11-A2)
- R28 pad 1: +3V3 -> Net-(D11-A2)
- R28 pad 2: Net-(J10-Pin_1) -> Net-(U13-CANL)
- R29 pad 1: Net-(J11-CC1) -> +3V3
- R29 pad 2: GND -> P1_19/ENET0_INT_N
- R30 pad 1: GND -> +3V3
- R30 pad 2: Net-(J11-CC2) -> P1_21/ENET0_MDIO
- R31 pad 2: /MCU IO Part 1/P0_6/ISPMODE_N -> P1_11/ENET0_NRST
- R32 pad 1: Net-(C25-Pad2) -> P0_31/ENET0_WAKE_IN_OUT
- R32 pad 2: /Ethernet PHY/ENET_TRX_M -> GND
- R33 pad 1: Net-(C27-Pad1) -> Net-(U15-TMS/GPIO0/CONFIG0)
- R33 pad 2: /Ethernet PHY/TRX_M -> Net-(D12-A)
- R34 pad 1: +3V3 -> Net-(U15-TDI/GPIO1)
- R34 pad 2: /Ethernet PHY/ENET0_NRST -> Net-(D13-A)
- R35 pad 1: +3V3 -> /Ethernet PHY/TRX_P
- R35 pad 2: /Ethernet PHY/P1_21/ENET0_MDIO -> Net-(C86-Pad1)
- R37 pad 1: +3V3 -> Net-(C88-Pad2)
- R37 pad 2: /Ethernet PHY/P1_19/ENET0_INT_N -> ENET0_TRX_M
- R38 pad 1: /Ethernet PHY/P0_31/ENET0_WAKE_IN_OUT -> Net-(C90-Pad1)
- R38 pad 2: GND -> /Ethernet PHY/TRX_M
- R39 pad 1: Net-(U5G-RESET_b) -> +3V3
- R39 pad 2: /MCU IO USB & Power/RESET_b -> Net-(U15-RXD2/GPIO4/CONFIG3)
- R4 pad 1: Net-(D9-A1) -> +BATT
- R4 pad 2: Net-(C20-Pad2) -> Net-(U3-EN/UVLO)
- R5 pad 1: Net-(C20-Pad2) -> Net-(U4-EN)
- R5 pad 2: Net-(D9-A2) -> Net-(U3-FB)
- R6 pad 1: Net-(U15-CANH) -> +5V
- R6 pad 2: Net-(D9-A1) -> Net-(U6-EN)
- R7 pad 1: Net-(D9-A2) -> +3V3
- R7 pad 2: Net-(U15-CANL) -> Net-(U6-FB)
- R8 pad 1: /Ethernet PHY/TRX_P -> +3V3
- R8 pad 2: Net-(C23-Pad1) -> Net-(D3-A)
- R9 pad 1: /Ethernet PHY/ENET_TRX_P -> +1V8
- R9 pad 2: Net-(C25-Pad2) -> Net-(D4-A)
- U1 pad 1: +5V -> Net-(U1-VCAP)
- U1 pad 2: unconnected-(U1-SW-Pad2)_1 -> GND
- U1 pad 3: unconnected-(U1-SW-Pad2)_2 -> Net-(Q1-S)
- U1 pad 4: unconnected-(U1-SW-Pad2) -> +BATT
- U1 pad 5: Net-(U1-EN) -> Net-(Q1-G)
- U1 pad 6: +3V3 -> Net-(Q1-S)
- U10 pad A2: /Sensors/P0_20/I3C0_SDA -> P0_20/I3C0_SDA
- U10 pad A3: /Sensors/P0_21/I3C0_SCL -> P0_21/I3C0_SCL
- U10 pad C1: +3V3 -> +1V8
- U11 pad 2: /Sensors/P0_21/I3C0_SCL -> P0_21/I3C0_SCL
- U11 pad 5: /Sensors/P0_20/I3C0_SDA -> P0_20/I3C0_SDA
- U13 pad 1: unconnected-(U13-SDO-Pad1) -> P4_16/CAN1_TXD
- U13 pad 3: /Communication/P0_8/FLEXIO0_D0 -> +5V
- U13 pad 4: /Communication/P0_9/FLEXIO0_D1 -> P4_15/CAN1_RXD
- U13 pad 5: +5V -> +3V3
- U13 pad 6: unconnected-(U13-CKO-Pad6) -> Net-(U13-CANL)
- U15 pad 1: /Communication/CAN1_TXD -> P1_20/ENET0_MDC
- U15 pad 2: GND -> P1_19/ENET0_INT_N
- U15 pad 3: +5V -> Net-(U15-VDD_CORE)
- U15 pad 4: /Communication/CAN1_RXD -> VDDIO
- U15 pad 5: +3V3 -> /Ethernet PHY/ENET0_XTAL_OUT
- U15 pad 6: Net-(U15-CANL) -> /Ethernet PHY/ENET0_XTAL_IN
- U15 pad 7: Net-(U15-CANH) -> Net-(U15-VDDA_AO)
- U15 pad 8: /Communication/MCU_P2_11 -> VDDA_TRX
- U15 pad 9: GND -> Net-(U15-VDDA_AO)
- U3 pad 11: Net-(C3-Pad2) -> Net-(C9-Pad2)
- U3 pad 12: Net-(C3-Pad2) -> Net-(C9-Pad2)
- Y1 pad 1: /Ethernet PHY/ENET0_XTAL_IN -> /MCU IO Part 1/EXTAL48M
- Y1 pad 3: /Ethernet PHY/ENET0_XTAL_OUT -> /MCU IO Part 1/XTAL48M
- Y3 pad 1: /MCU IO Part 1/EXTAL48M -> /Ethernet PHY/ENET0_XTAL_IN
- Y3 pad 3: /MCU IO Part 1/XTAL48M -> /Ethernet PHY/ENET0_XTAL_OUT
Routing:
- net +3V3: track 0.00 -> 29.3 mm, vias 0 -> 6
- net GND: track 0.00 -> 18.0 mm, vias 0 -> 15
- net Net-(U7H-VDD_CORE_1): track 0.00 -> 9.30 mm, vias 0 -> 2
- net P0_31/ENET0_WAKE_IN_OUT: track 0.00 -> 5.80 mm, vias 0 -> 1
- net P1_21/ENET0_MDIO: track 0.00 -> 5.47 mm, vias 0 -> 1
- net P1_19/ENET0_INT_N: track 0.00 -> 5.47 mm, vias 0 -> 1
- net P1_16/FC3_P4: track 0.00 -> 5.30 mm, vias 0 -> 1
- net P1_23/FC4_P3: track 0.00 -> 4.84 mm, vias 0 -> 1
- net P1_17/FC3_P5: track 0.00 -> 4.84 mm, vias 0 -> 1
- net Net-(U7H-VDD_ANA): track 0.00 -> 4.72 mm
- net P3_4/FC7_P2: track 0.00 -> 4.40 mm, vias 0 -> 1
- net P1_20/ENET0_MDC: track 0.00 -> 4.30 mm, vias 0 -> 1
- net P4_14/CAN0_STB: track 0.00 -> 4.20 mm, vias 0 -> 1
- net P1_22/FC4_P2: track 0.00 -> 3.80 mm, vias 0 -> 1
- net P1_18/FC3_P6: track 0.00 -> 3.80 mm, vias 0 -> 1
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
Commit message: Updated PCB layout
- Placed decoupling caps at MCXN with traces.
- Grouped parts of schematic.
- Started positioning Power components
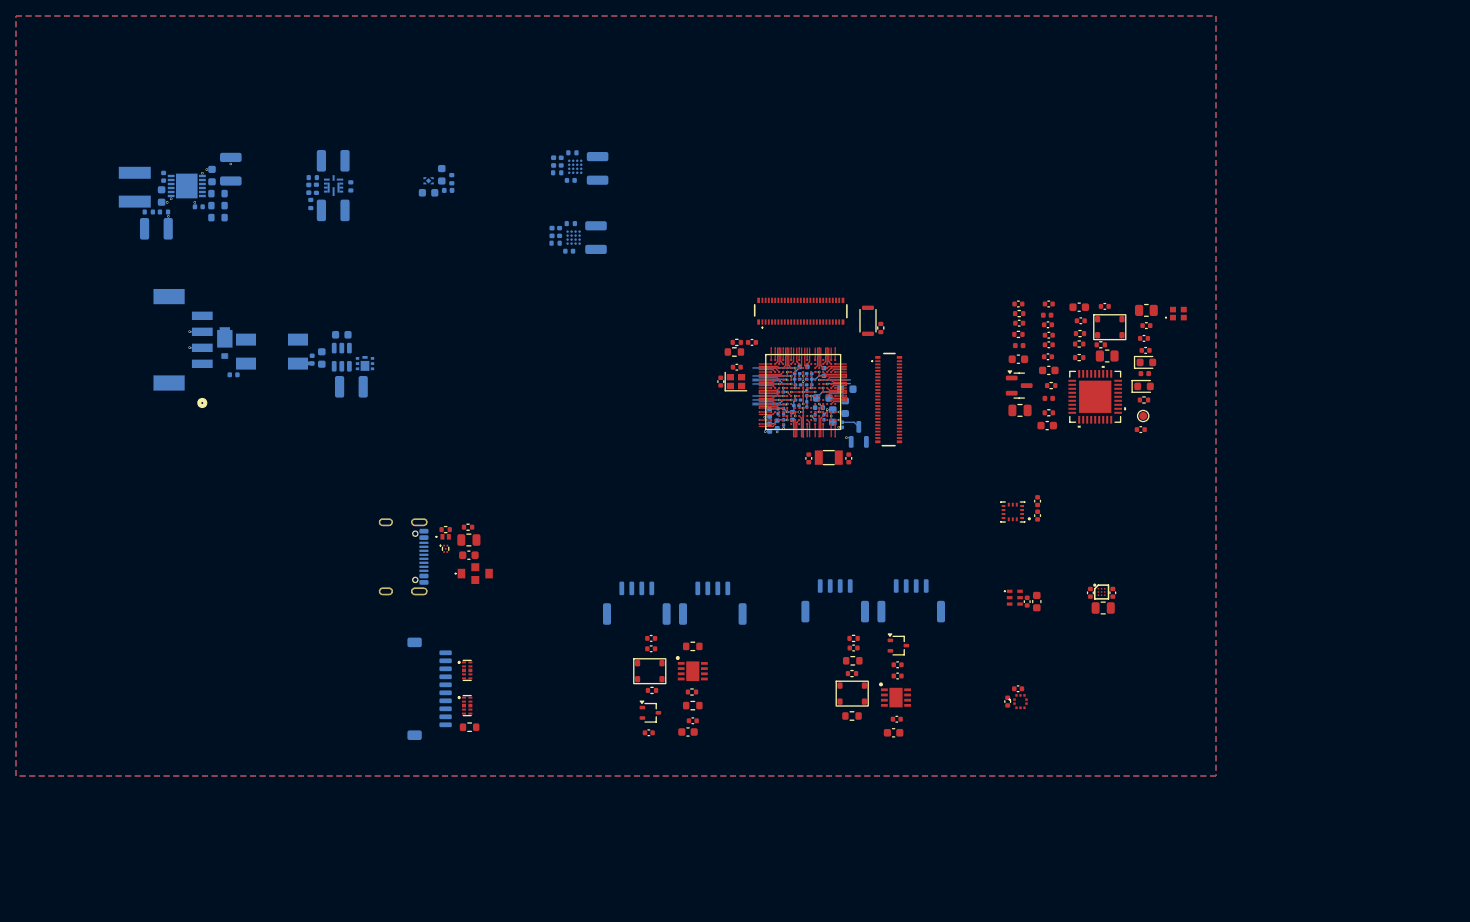
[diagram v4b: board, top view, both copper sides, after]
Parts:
- C1, C10, C11, C12, C13, C14, C15, C16, C17, C18, C19, C2, C20, C21, C3, C4, C47, C5, C6, C7, C8, C9, D1, D2, D3, D4, D5, J1, J2, J3, J4, J5, J6, J7, L1, L2, Q1, R1, R10, R11, R12, R13, R14, R2, R3, R4, R5, R6, R7, R8, R9, U1, U2, U3, U4, U5, U6: moved to B.Cu
- L4: value 1.5uH -> 1uH; footprint Inductor_SMD:L_1008_2520Metric -> Inductor_SMD:L_0603_1608Metric; moved to B.Cu
- moved R12 153.0 mm to (53.5, 74.5)
- moved C20 151.4 mm to (53.2, 72.5), turned to 90 degrees
- moved R3 147.0 mm to (60.2, 72.2), turned to 180 degrees
- moved C9 142.2 mm to (53.5, 70.1), turned to 90 degrees
- moved R13 141.0 mm to (72.1, 70.2), turned to 180 degrees
- moved C19 139.8 mm to (57.9, 73.8)
- moved L2 139.4 mm to (49.9, 71.4), turned to -90 degrees
- moved R7 136.3 mm to (72.5, 71.6), turned to 90 degrees
- moved D1 134.0 mm to (61.1, 91.5), turned to -90 degrees
- moved R11 132.6 mm to (60.2, 75.2)
- moved C15 131.9 mm to (74.7, 68.1)
- moved R6 131.7 mm to (76.8, 71.3), turned to -90 degrees
- moved C12 129.8 mm to (52.5, 76.6), turned to 180 degrees
- moved R5 126.0 mm to (51.6, 74.5)
- moved C11 125.0 mm to (59.5, 70.0), turned to -90 degrees
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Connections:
- D9 pad 2: P0_4 -> P0_4/DEBUG_GPIO
- D9 pad 9: P0_4 -> P0_4/DEBUG_GPIO
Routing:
- net +3V3: track 29.3 -> 56.2 mm, vias 6 -> 8
- net Net-(U7H-VDD_CORE_1): track 9.30 -> 17.1 mm
- net Net-(U7H-VDD_BAT): track 1.40 -> 3.31 mm, vias 0 -> 1
- net Net-(Q1-S): track 0.00 -> 1.78 mm
- net ENET0_TRX_P: track 0.00 -> 1.60 mm, vias 0 -> 1
- net ENET0_TRX_M: track 0.00 -> 1.60 mm, vias 0 -> 1
- net Net-(U7H-VDD_ANA): track 4.72 -> 3.41 mm, vias 0 -> 1
- net ANA_6/DAC2_OUT: track 1.30 -> 2.12 mm
- net Net-(U7H-VDD_SYS/VOUT_SYS): track 0.71 -> 1.34 mm
- net Net-(U7H-DCDC_LX/DCDC_LX): track 1.48 -> 1.33 mm, vias 0 -> 1
- net GND: vias 15 -> 26
- added copper zone on B.Cu, net GND
- added copper zone on F.Cu, net GND
- added copper zone on In1.Cu, net GND
